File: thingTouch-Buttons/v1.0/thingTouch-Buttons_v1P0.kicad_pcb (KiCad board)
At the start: 2 copper layers, 160 x 48 mm, 23 parts, among them P1 DIRECT_CONN, P2 TOUCH_CONN, U1 TTP224N-BSB

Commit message: final routing done; verification left
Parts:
- added REF**: VIA_0.6mm, via:VIA_0.6mm, F.Cu at (166.8, 92.0)
- added REF**: VIA_0.6mm, via:VIA_0.6mm, F.Cu at (74.0, 93.4)
- added REF**: VIA_0.6mm, via:VIA_0.6mm, F.Cu at (71.7, 88.8)
- added REF**: VIA_0.6mm, via:VIA_0.6mm, F.Cu at (74.0, 82.2)
- added REF**: VIA_0.6mm, via:VIA_0.6mm, F.Cu at (84.3, 82.2)
- added REF**: VIA_0.6mm, via:VIA_0.6mm, F.Cu at (93.5, 82.2)
- added REF**: VIA_0.6mm, via:VIA_0.6mm, F.Cu at (104.0, 82.2)
- added REF**: VIA_0.6mm, via:VIA_0.6mm, F.Cu at (111.6, 82.2)
- added REF**: VIA_0.6mm, via:VIA_0.6mm, F.Cu at (111.6, 88.5)
- added REF**: VIA_0.6mm, via:VIA_0.6mm, F.Cu at (124.2, 92.7)
- added REF**: VIA_0.6mm, via:VIA_0.6mm, F.Cu at (223.8, 93.6)
- added REF**: VIA_0.6mm, via:VIA_0.6mm, F.Cu at (170.8, 92.0)
- added REF**: VIA_0.6mm, via:VIA_0.6mm, F.Cu at (223.8, 88.0)
- added REF**: VIA_0.6mm, via:VIA_0.6mm, F.Cu at (223.8, 83.0)
- added REF**: VIA_0.6mm, via:VIA_0.6mm, F.Cu at (189.6, 81.9)
- added REF**: VIA_0.6mm, via:VIA_0.6mm, F.Cu at (189.6, 86.5)
- added REF**: VIA_0.6mm, via:VIA_0.6mm, F.Cu at (153.9, 92.7)
- added REF**: VIA_0.6mm, via:VIA_0.6mm, F.Cu at (120.2, 92.7)
- added REF**: VIA_0.6mm, via:VIA_0.6mm, F.Cu at (142.4, 82.5)
- added REF**: VIA_0.6mm, via:VIA_0.6mm, F.Cu at (170.8, 87.8)
- added REF**: VIA_0.6mm, via:VIA_0.6mm, F.Cu at (166.8, 87.8)
- added REF**: VIA_0.6mm, via:VIA_0.6mm, F.Cu at (170.8, 82.5)
- added REF**: VIA_0.6mm, via:VIA_0.6mm, F.Cu at (157.3, 82.5)
- added REF**: VIA_0.6mm, via:VIA_0.6mm, F.Cu at (131.6, 82.5)
- added REF**: VIA_0.6mm, via:VIA_0.6mm, F.Cu at (93.4, 93.4)
- added REF**: VIA_0.6mm, via:VIA_0.6mm, F.Cu at (84.4, 93.4)
- P1: footprint Connectors_JST:JST_PH_S4B-PH-SM4-TB_04x2.00mm_Angled -> Connectors_JST:JST_PH_S6B-PH-SM4-TB_06x2.00mm_Angled
- moved R3 2.09 mm to (138.6, 92.2)
- moved R1 2.06 mm to (138.6, 87.4)
- moved C2 2.06 mm to (134.9, 99.9)
- moved R2 1.79 mm to (138.6, 90.0)
- moved C5 1.63 mm to (147.3, 83.7)
- moved C4 1.23 mm to (152.4, 83.8)
- moved R6 0.79 mm to (160.6, 92.2)
- moved R5 0.76 mm to (160.6, 90.0)
- moved R4 0.56 mm to (160.6, 87.8)
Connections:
- P1 pad 1: GND -> Net-(C3-Pad1)
- P1 pad 2: Net-(C3-Pad1) -> GND
- P1 pad 4: Net-(C1-Pad1) -> GND
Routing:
- net (no net): track 1620.8 -> 417.8 mm
- net Net-(C3-Pad1): track 125.2 -> 97.9 mm, vias 1 -> 3
- net VDD: track 53.4 -> 60.4 mm
- net Net-(D3-Pad2): track 63.7 -> 58.7 mm
- net Net-(D2-Pad2): track 64.1 -> 59.8 mm
- net Net-(D1-Pad2): track 64.3 -> 61.4 mm
- net Net-(C2-Pad1): track 71.7 -> 69.5 mm
- net GND: track 12.9 -> 14.9 mm, vias 2 -> 0
- net Net-(C1-Pad1): track 73.6 -> 75.4 mm
- net Net-(R3-Pad1): track 9.53 -> 8.27 mm
- net Net-(R2-Pad1): track 8.52 -> 7.69 mm

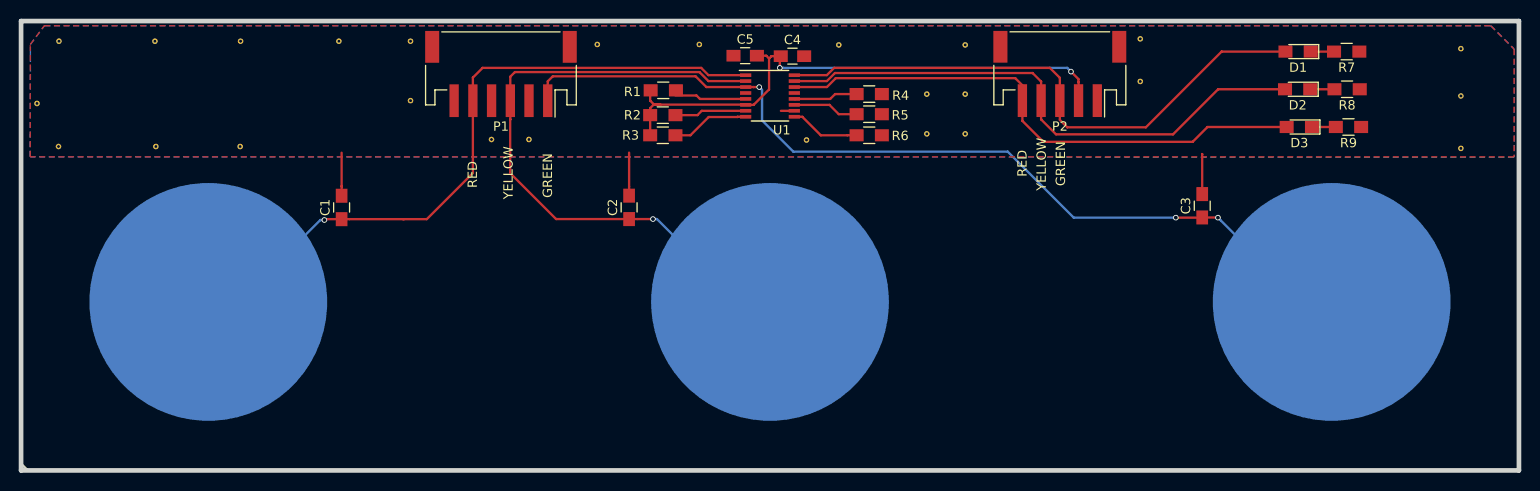
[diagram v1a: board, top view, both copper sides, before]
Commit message: following changes are done
Layout following changes done
-> 2.0mm mounting holes added
-> company logo and name
-> fab details
-> rerouting of touch signals and VDD signals
-> Bom created
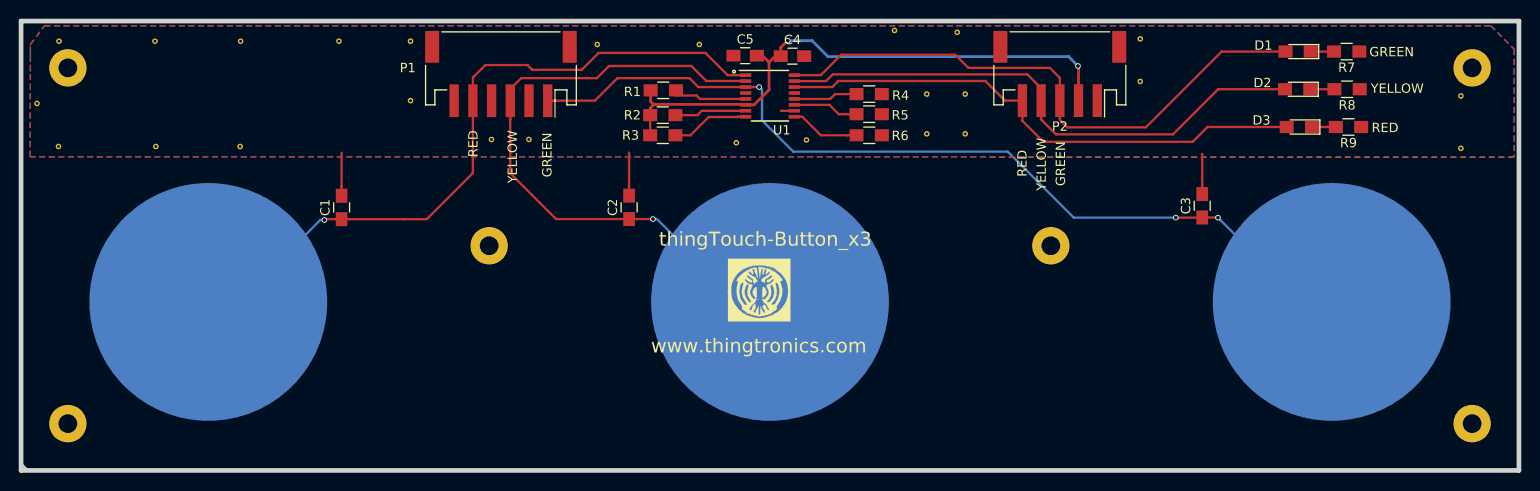
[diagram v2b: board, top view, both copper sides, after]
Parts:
- added G***: LOGO, logos:thingTronics_10mm, F.Cu at (148.8, 108.7)
- added REF**: MountingHole_2.0mm_Pad, Mounting_Holes:MountingHole_3.5mm_Pad, F.Cu at (180.0, 110.0)
- added REF**: MountingHole_2.0mm_Pad, Mounting_Holes:MountingHole_3.5mm_Pad, F.Cu at (120.3, 110.0)
- added REF**: Fab Details table, Fab Details table:Fab Details table, F.Cu at (33.6, 81.5)
- added REF**: MountingHole_2.0mm_Pad, Mounting_Holes:MountingHole_3.5mm_Pad, F.Cu at (75.9, 85.2)
- added REF**: MountingHole_2.0mm_Pad, Mounting_Holes:MountingHole_3.5mm_Pad, F.Cu at (226.9, 86.3)
- added REF**: MountingHole_2.0mm_Pad, Mounting_Holes:MountingHole_3.5mm_Pad, F.Cu at (226.4, 125.2)
- added REF**: MountingHole_2.0mm_Pad, Mounting_Holes:MountingHole_3.5mm_Pad, F.Cu at (75.5, 124.1)
- moved REF** 78.0 mm to (146.4, 93.0)
- moved REF** 6.15 mm to (163.3, 81.0)
- moved REF** 1.60 mm to (170.0, 81.2)
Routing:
- net VDD: track 60.4 -> 62.5 mm
- net Net-(C1-Pad1): track 75.4 -> 77.2 mm
- net Net-(C3-Pad1): track 97.9 -> 96.6 mm
- net Net-(D3-Pad2): track 58.7 -> 57.5 mm
- net Net-(D1-Pad2): track 61.4 -> 62.6 mm
- net Net-(D2-Pad2): track 59.8 -> 59.3 mm
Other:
- net class PWR added: clearance 0.2, trace_width 0.3, via_dia 0.6, via_drill 0.4
- board text added: "160x48"
- board text added: "thingTouch-Button_x3"
- board text added: "www.thingtronics.com"

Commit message: verified the layout
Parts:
- moved REF** 1.03 mm to (142.7, 81.5)
- moved REF** 0.95 mm to (131.6, 81.5)
- moved REF** 0.20 mm to (163.3, 81.2)
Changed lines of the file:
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@@
       (effects (font (size 1 1) (thickness 0.15)))
     )
-    (fp_text value MountingHole_2.0mm_Pad (at 0 4.5) (layer F.Fab)
+    (fp_text value MountingHole_2.0mm_Pad (at -7.2 9.25) (layer F.Fab)
       (effects (font (size 1 1) (thickness 0.15)))
     )
@@
       (effects (font (size 1 1) (thickness 0.15)))
     )
-    (fp_text value MountingHole_2.0mm_Pad (at 0 4.5) (layer F.Fab)
+    (fp_text value MountingHole_2.0mm_Pad (at -7.6 1.45) (layer F.Fab)
       (effects (font (size 1 1) (thickness 0.15)))
     )
@@
       (effects (font (size 1 1) (thickness 0.15)))
     )
-    (fp_text value MountingHole_2.0mm_Pad (at 0 4.5) (layer F.Fab)
+    (fp_text value MountingHole_2.0mm_Pad (at 4.95 2.45) (layer F.Fab)
       (effects (font (size 1 1) (thickness 0.15)))
     )
@@
   )
   (module via:VIA_0.6mm (layer F.Cu)
-    (at 163.3 81)
-    (fp_text reference REF** (at 0 -2.6) (layer F.Fab) hide
-      (effects (font (size 1 1) (thickness 0.15)))
-    )
-    (fp_text value VIA_0.6mm (at 0.05 -1.45) (layer F.Fab) hide
-      (effects (font (size 1 1) (thickness 0.15)))
-    )
-    (pad 1 thru_hole circle (at 0 0) (size 0.6 0.6) (drill 0.3) (layers *.Cu)
-      (net 2 GND) (zone_connect 2))
-  )
-  (module via:VIA_0.6mm (layer F.Cu)
-    (at 131.55 82.5)
+    (at 163.3 81.2)
+    (fp_text reference REF** (at 0 -2.6) (layer F.Fab) hide
+      (effects (font (size 1 1) (thickness 0.15)))
+    )
+    (fp_text value VIA_0.6mm (at 0.05 -1.45) (layer F.Fab) hide
+      (effects (font (size 1 1) (thickness 0.15)))
+    )
+    (pad 1 thru_hole circle (at 0 0) (size 0.6 0.6) (drill 0.3) (layers *.Cu)
+      (net 2 GND) (zone_connect 2))
+  )
+  (module via:VIA_0.6mm (layer F.Cu)
+    (at 131.55 81.55)
     (fp_text reference REF** (at 0 -2.6) (layer F.Fab) hide
       (effects (font (size 1 1) (thickness 0.15)))
@@
   )
   (module via:VIA_0.6mm (layer F.Cu)
-    (at 142.45 82.5)
+    (at 142.7 81.5)
     (fp_text reference REF** (at 0 -2.6) (layer F.Fab) hide
       (effects (font (size 1 1) (thickness 0.15)))
@@
       (effects (font (size 1 1) (thickness 0.15)))
     )
-    (fp_text value MountingHole_2.0mm_Pad (at 0 4.5) (layer F.Fab)
+    (fp_text value MountingHole_2.0mm_Pad (at 6.55 3.75) (layer F.Fab)
       (effects (font (size 1 1) (thickness 0.15)))
     )
@@
   )
   (gr_circle (center 146.158579 85.4) (end 146.258579 85.5) (layer F.SilkS) (width 0.15))
-  (gr_text GREEN (at 216.4 83.3 360) (layer F.SilkS)
+  (gr_text GREEN (at 216.4 83.3) (layer F.SilkS)
     (effects (font (size 1 1) (thickness 0.15)))
   )
-  (gr_text YELLOW (at 217 87.2 360) (layer F.SilkS)
+  (gr_text YELLOW (at 217 87.2) (layer F.SilkS)
     (effects (font (size 1 1) (thickness 0.15)))
   )
-  (gr_text RED (at 215.7 91.4 360) (layer F.SilkS)
+  (gr_text RED (at 215.7 91.4) (layer F.SilkS)
     (effects (font (size 1 1) (thickness 0.15)))
   )
